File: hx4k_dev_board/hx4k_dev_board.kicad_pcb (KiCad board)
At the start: 4 copper layers, 85 x 54 mm, 111 parts, among them J1 USB_B, J2 RB1-125B8G1A, J3 Conn_01x08, J4 Conn_02x06_Odd_Even, J5 Conn_02x06_Odd_Even, SW1 SW_SPST, SW2 SW_SPST, SW3 SW_SPST, U1 W9812G6KH-6, U2 CH340E, U3 TPS7A7001DDA, U4 TPS7A7001DDA, U5 RTL8211EG-VB-CG, U6 ICE40HX4K-TQ144, U7 W25Q128JVS, X1 SG-7050CAN, X2 SG-7050CAN

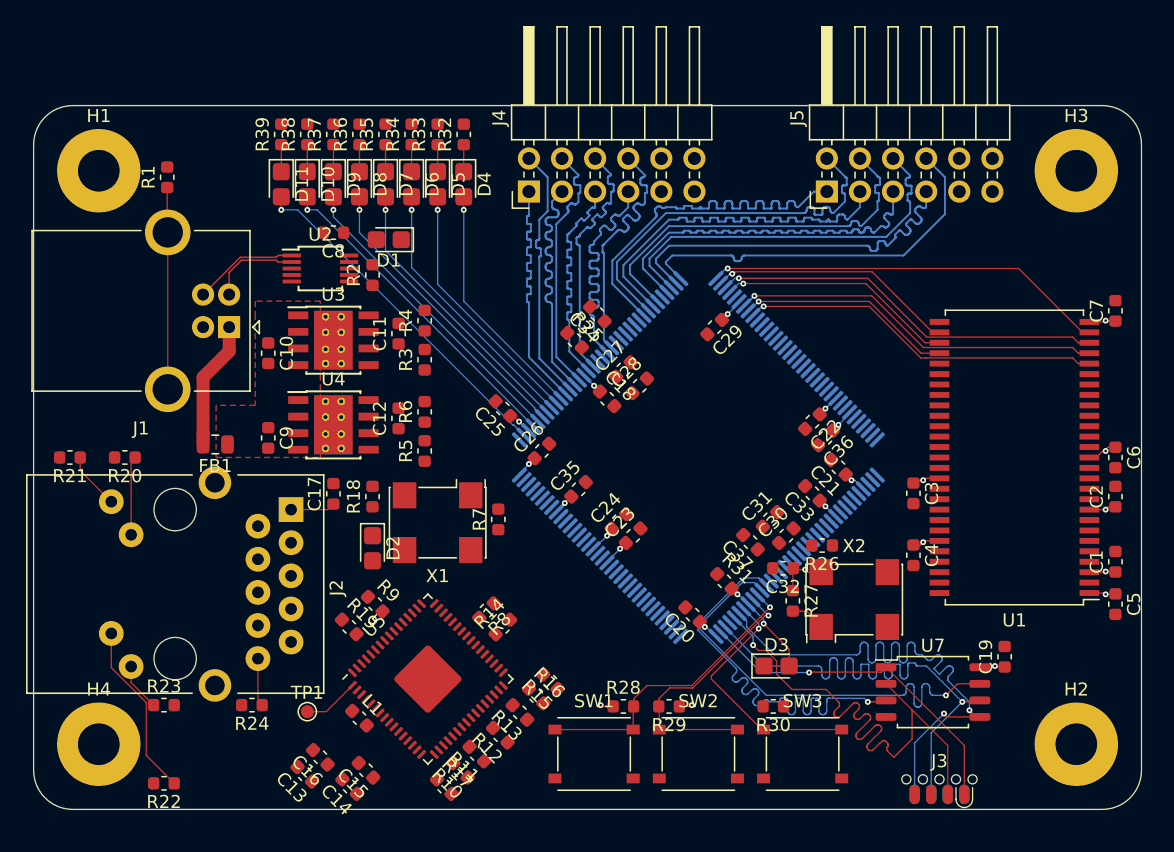
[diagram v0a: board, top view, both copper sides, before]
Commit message: Pre tuning of DDR length matching
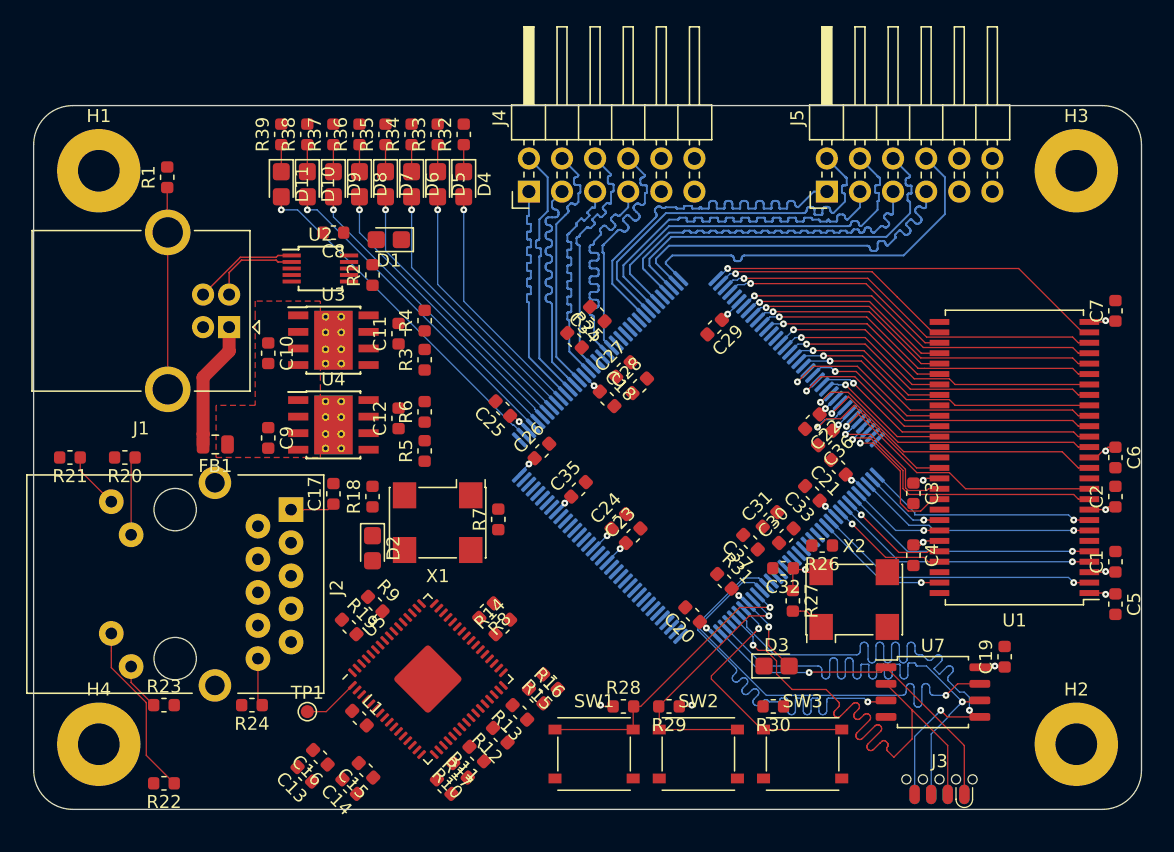
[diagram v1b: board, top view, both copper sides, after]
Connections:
- U6 pad 19: Net-(U6-Pad19) -> /SDRAM/~CS
- U6 pad 20: Net-(U6-Pad20) -> /FPGA/~RAM_RAS
- U6 pad 21: Net-(U6-Pad21) -> /SDRAM/CKE
- U6 pad 22: Net-(U6-Pad22) -> /SDRAM/~CAS
- U6 pad 23: Net-(U6-Pad23) -> /SDRAM/CLK
- U6 pad 24: Net-(U6-Pad24) -> /FPGA/~RAM_WE
- U6 pad 25: Net-(U6-Pad25) -> /FPGA/RAM_UDQM
- U6 pad 26: Net-(U6-Pad26) -> /SDRAM/LDQM
- U6 pad 28: Net-(U6-Pad28) -> /SDRAM/DATA7
- U6 pad 29: Net-(U6-Pad29) -> /SDRAM/DATA8
- U6 pad 31: Net-(U6-Pad31) -> /SDRAM/DATA6
- U6 pad 32: Net-(U6-Pad32) -> /SDRAM/DATA9
- U6 pad 33: Net-(U6-Pad33) -> /SDRAM/DATA5
- U6 pad 34: Net-(U6-Pad34) -> /SDRAM/DATA10
- U6 pad 37: Net-(U6-Pad37) -> /SDRAM/DATA4
- U6 pad 38: Net-(U6-Pad38) -> /SDRAM/DATA11
- U6 pad 39: /SDRAM/~CS -> /SDRAM/DATA3
- U6 pad 41: /SDRAM/CKE -> /SDRAM/DATA12
- U6 pad 42: /SDRAM/CLK -> /SDRAM/DATA2
- U6 pad 43: /SDRAM/LDQM -> /SDRAM/DATA13
- U6 pad 44: /FPGA/RAM_UDQM -> /SDRAM/DATA1
- U6 pad 45: /FPGA/~RAM_WE -> /SDRAM/DATA14
- U6 pad 47: /SDRAM/~CAS -> /SDRAM/DATA0
- U6 pad 48: /FPGA/~RAM_RAS -> /SDRAM/DATA15
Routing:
- net /SDRAM/ADDRESS10: track 0.00 -> 27.2 mm, vias 0 -> 1
- net /SDRAM/BS1: track 0.00 -> 25.9 mm, vias 0 -> 1
- net /SDRAM/BS0: track 0.00 -> 24.9 mm, vias 0 -> 1
- net /SDRAM/~CS: track 0.00 -> 24.0 mm, vias 0 -> 1
- net /FPGA/~RAM_RAS: track 0.00 -> 23.8 mm, vias 0 -> 1
- net /SDRAM/LDQM: track 0.00 -> 23.8 mm, vias 0 -> 1
- net /SDRAM/DATA7: track 0.00 -> 23.7 mm, vias 0 -> 1
- net /SDRAM/~CAS: track 0.00 -> 23.3 mm, vias 0 -> 1
- net /SDRAM/DATA6: track 0.00 -> 22.5 mm, vias 0 -> 1
- net /FPGA/~RAM_WE: track 0.00 -> 22.5 mm, vias 0 -> 1
- net /SDRAM/DATA5: track 0.00 -> 22.4 mm, vias 0 -> 1
- net /SDRAM/DATA0: track 0.00 -> 21.8 mm, vias 0 -> 1
- net /SDRAM/DATA1: track 0.00 -> 20.5 mm, vias 0 -> 1
- net /SDRAM/DATA2: track 0.00 -> 19.7 mm, vias 0 -> 1
- net /SDRAM/DATA3: track 0.00 -> 18.4 mm, vias 0 -> 1
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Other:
- net class 100R diff: via_dia 0.45 -> 0.53
- net class 50R: via_dia 0.45 -> 0.53
- net class 90R: via_dia 0.45 -> 0.53
- net class Default: via_dia 0.45 -> 0.53
- rule via_min_size: 0.45 -> 0.53

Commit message: Fully routed
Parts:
- removed R8: 10k, Resistor_SMD:R_0603_1608Metric
- U5: footprint Package_DFN_QFN:QFN-64-1EP_9x9mm_P0.5mm_EP3.8x3.8mm -> Package_DFN_QFN:QFN-64-1EP_9x9mm_P0.5mm_EP3.8x3.8mm_ThermalVias
- moved C14 12.7 mm to (316.9, 84.6), turned to 45 degrees
- moved R11 12.6 mm to (337.6, 88.0)
- moved R12 11.8 mm to (338.4, 86.5)
- moved R14 11.7 mm to (336.1, 75.7)
- moved R10 11.2 mm to (335.4, 90.3)
- moved C13 10.2 mm to (317.1, 86.7), turned to 45 degrees
- moved R25 8.28 mm to (340.6, 68.6), turned to 135 degrees
- moved R16 7.58 mm to (336.3, 84.4)
- moved R26 6.82 mm to (347.4, 75.7), turned to 315 degrees
- moved R13 6.16 mm to (334.9, 87.5)
- moved R15 4.36 mm to (335.5, 85.9)
- moved D1 4.22 mm to (323.1, 58.4)
- moved C15 3.34 mm to (316.9, 93.0)
- moved R9 2.61 mm to (321.6, 82.2), turned to 225 degrees
- moved R30 2.33 mm to (347.4, 91.3), turned to 0 degrees
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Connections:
- net /POWER/1V8FB renamed /POWER/1V2FB
- net Net-(C27-Pad1) renamed /FPGA/VCCPLL1
- net Net-(C27-Pad2) renamed /FPGA/GNDPLL1
- net Net-(C30-Pad1) renamed /FPGA/VCCPLL0
- net Net-(C30-Pad2) renamed /FPGA/GNDPLL0
- U6 pad 101: /ETHERNET/COL -> /FPGA/ETH_TXD6
- U6 pad 102: /ETHERNET/CS -> /FPGA/ETH_TXD7
- U6 pad 104: /FPGA/ETH_MDC -> /FPGA/ETH_TXER
- U6 pad 107: /FPGA/~ETH_PHYRST -> /FPGA/ETH_MDC
- U6 pad 73: /FPGA/ETH_GTXCLK -> /FPGA/ETH_RXDV
- U6 pad 74: /FPGA/ETH_TXCLK -> /FPGA/ETH_RXD0
- U6 pad 75: /FPGA/ETH_TXD0 -> /FPGA/ETH_RXD1
- U6 pad 76: /FPGA/ETH_TXD1 -> /FPGA/ETH_RXD2
- U6 pad 78: /FPGA/ETH_TXD2 -> /FPGA/ETH_RXD3
- U6 pad 79: /FPGA/ETH_TXD3 -> /ETHERNET/RXCLK
- U6 pad 80: /FPGA/ETH_TXD4 -> /FPGA/ETH_RXD4
- U6 pad 81: /FPGA/ETH_TXD5 -> /FPGA/ETH_RXD5
- U6 pad 82: /FPGA/ETH_TXD6 -> /FPGA/ETH_RXD6
- U6 pad 83: /FPGA/ETH_TXD7 -> /FPGA/ETH_RXD7
- U6 pad 84: /FPGA/ETH_TXEN -> /FPGA/ETH_RXER
- U6 pad 85: /FPGA/ETH_TXER -> /ETHERNET/COL
- U6 pad 87: /ETHERNET/RXCLK -> /ETHERNET/CS
- U6 pad 88: /FPGA/ETH_RXD0 -> /FPGA/ETH_GTXCLK
- U6 pad 90: /FPGA/ETH_RXD1 -> /FPGA/ETH_TXEN
- U6 pad 91: /FPGA/ETH_RXD2 -> /FPGA/ETH_TXD0
- U6 pad 93: /FPGA/ETH_RXD3 -> /FPGA/~ETH_PHYRST
- U6 pad 94: /FPGA/ETH_RXD4 -> /FPGA/ETH_TXD1
- U6 pad 95: /FPGA/ETH_RXD5 -> /FPGA/ETH_TXD2
- U6 pad 96: /FPGA/ETH_RXD6 -> /FPGA/ETH_TXD3
- U6 pad 97: /FPGA/ETH_RXD7 -> /FPGA/ETH_TXCLK
- U6 pad 98: /FPGA/ETH_RXDV -> /FPGA/ETH_TXD4
- U6 pad 99: /FPGA/ETH_RXER -> /FPGA/ETH_TXD5
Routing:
- net GND: track 0.00 -> 84.6 mm, vias 0 -> 74
- net /USB_UART/UART_RX: track 0.00 -> 48.1 mm, vias 0 -> 1
- net /FPGA/UART_CTS: track 0.00 -> 47.3 mm, vias 0 -> 1
- net /FPGA/~UART_RTS: track 0.00 -> 46.5 mm, vias 0 -> 1
- net /FPGA/UART_RX: track 0.00 -> 44.2 mm, vias 0 -> 1
- net +3V3: track 37.6 -> 68.7 mm, vias 19 -> 50
- net /ETHERNET/LED_G_HIGH: track 4.38 -> 34.0 mm
- net /ETHERNET/LED_Y_HIGH: track 13.5 -> 40.5 mm
- net /ETHERNET/MDI2_P: track 0.00 -> 25.7 mm, vias 0 -> 1
- net /FPGA/ETH_RXDV: track 0.00 -> 24.9 mm, vias 0 -> 1
- net /SDRAM/DATA11: track 6.41 -> 31.2 mm
- net /FPGA/ETH_MDC: track 0.00 -> 24.2 mm, vias 0 -> 1
- net /SDRAM/DATA12: track 7.36 -> 31.0 mm
- net /FPGA/~ETH_PME_INT: track 0.00 -> 23.6 mm, vias 0 -> 1
- net /ETHERNET/MDI2_N: track 0.00 -> 23.3 mm, vias 0 -> 1
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- added copper zone on B.Cu, net +1V2
- added copper zone on F.Cu, net +1V2
- added copper zone on F.Cu, net +3V3
- added copper zone on In2.Cu, net +3V3
- added copper zone on F.Cu, net /ETHERNET/VDD
- added copper zone on F.Cu, net GND
- added copper zone on In1.Cu, net GND
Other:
- net class Power added: clearance 0.0889, trace_width 0.3, via_dia 0.53, via_drill 0.2

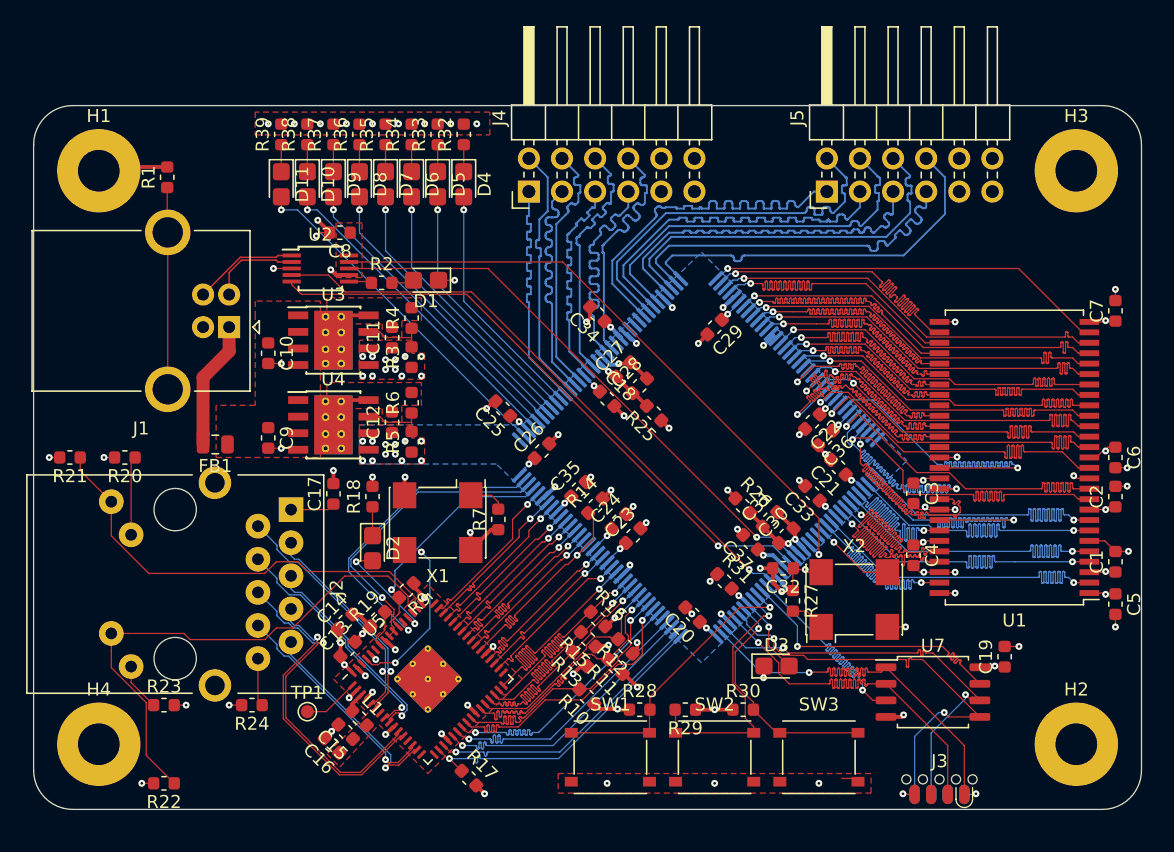
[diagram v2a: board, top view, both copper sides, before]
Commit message: PMODs corrected
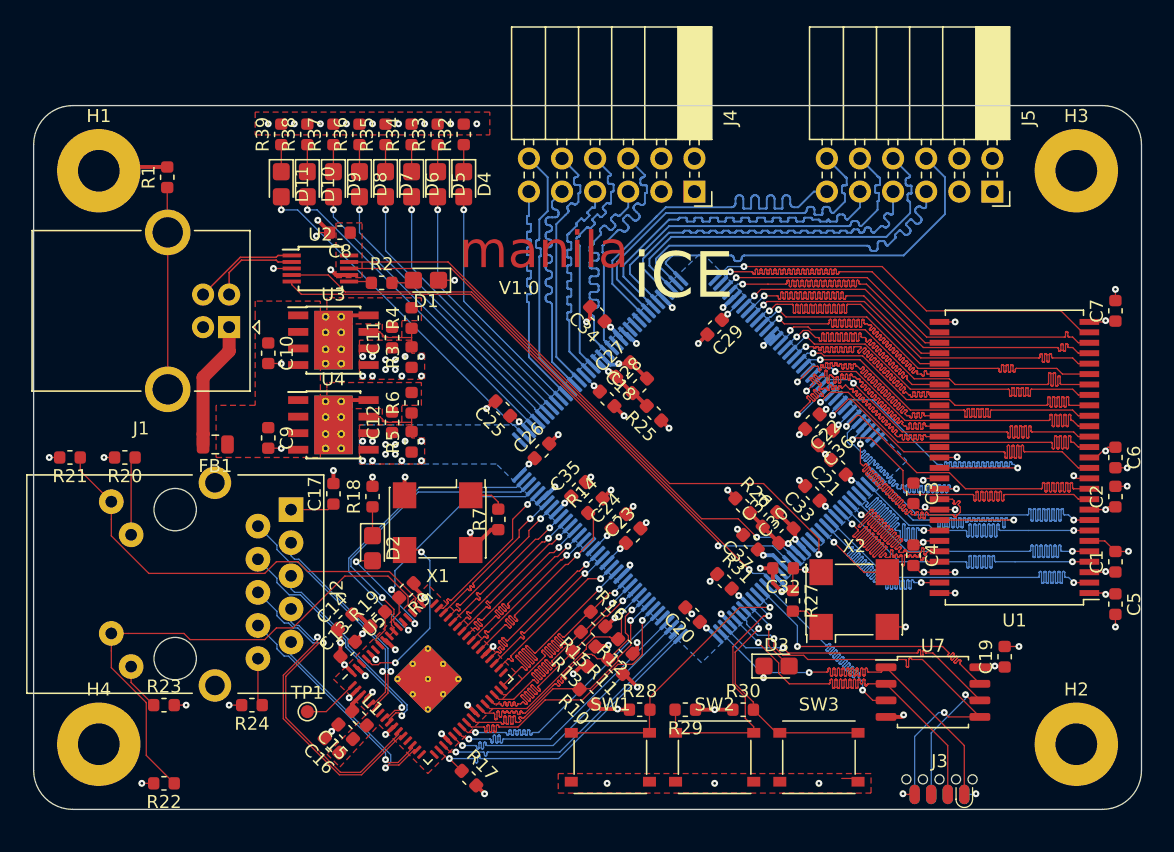
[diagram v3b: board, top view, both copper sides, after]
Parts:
- J4, J5: footprint Connector_PinHeader_2.54mm:PinHeader_2x06_P2.54mm_Horizontal -> Connector_PinSocket_2.54mm:PinSocket_2x06_P2.54mm_Horizontal
- moved J4 12.7 mm to (343.7, 51.6), turned to 270 degrees
- moved J5 12.7 mm to (366.6, 51.6), turned to 270 degrees
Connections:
- J4 pad 1: /PMODA/DATA0 -> +3V3
- J4 pad 10: GND -> /PMODA/DATA3
- J4 pad 11: +3V3 -> /PMODA/DATA0
- J4 pad 12: +3V3 -> /PMODA/DATA1
- J4 pad 2: /PMODA/DATA1 -> +3V3
- J4 pad 3: /PMODA/DATA2 -> GND
- J4 pad 4: /PMODA/DATA3 -> GND
- J4 pad 5: /PMODA/DATA4 -> /PMODA/DATA6
- J4 pad 6: /PMODA/DATA5 -> /PMODA/DATA7
- J4 pad 7: /PMODA/DATA6 -> /PMODA/DATA4
- J4 pad 8: /PMODA/DATA7 -> /PMODA/DATA5
- J4 pad 9: GND -> /PMODA/DATA2
- J5 pad 1: /PMODB/DATA0 -> +3V3
- J5 pad 10: GND -> /PMODB/DATA3
- J5 pad 11: +3V3 -> /PMODB/DATA0
- J5 pad 12: +3V3 -> /PMODB/DATA1
- J5 pad 2: /PMODB/DATA1 -> +3V3
- J5 pad 3: /PMODB/DATA2 -> GND
- J5 pad 4: /PMODB/DATA3 -> GND
- J5 pad 5: /PMODB/DATA4 -> /PMODB/DATA6
- J5 pad 6: /PMODB/DATA5 -> /PMODB/DATA7
- J5 pad 7: /PMODB/DATA6 -> /PMODB/DATA4
- J5 pad 8: /PMODB/DATA7 -> /PMODB/DATA5
- J5 pad 9: GND -> /PMODB/DATA2
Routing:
- net /SDRAM/ADDRESS11: track 28.0 -> 31.2 mm
- net /SDRAM/CKE: track 28.6 -> 31.1 mm
- net /SDRAM/ADDRESS4: track 32.6 -> 31.0 mm
- net /USB_UART/UART_RX: track 48.1 -> 47.2 mm
- net /SDRAM/ADDRESS8: track 31.0 -> 32.0 mm
- net /SDRAM/~CS: track 31.1 -> 31.7 mm
- net /FPGA/~RAM_RAS: track 31.1 -> 31.6 mm
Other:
- board text added: "V1.0"
- board text added: "iCE"
- board text added: "manila"

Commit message: Basically done.
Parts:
- added G***: LOGO, Art:Shetland_combined, B.Cu at (370.0, 66.5)
- added REF**: KiCad-Logo2_5mm_SilkScreen, Symbol:KiCad-Logo2_5mm_SilkScreen, B.Cu at (309.0, 94.5)
- added REF**: OSHW-Logo_5.7x6mm_SilkScreen, Symbol:OSHW-Logo_5.7x6mm_SilkScreen, F.Cu at (368.2, 57.0)
- added TP2: TestPoint, TestPoint:TestPoint_Pad_D1.0mm, F.Cu at (326.5, 65.2)
- added TP3: TestPoint, TestPoint:TestPoint_Pad_D1.0mm, F.Cu at (326.8, 71.5)
- added TP4: TestPoint, TestPoint:TestPoint_Pad_D1.0mm, F.Cu at (294.0, 69.2)
- moved H2 44.0 mm to (373.0, 50.0)
- moved H3 44.0 mm to (373.0, 94.0)
- moved R1 4.69 mm to (306.6, 53.8), turned to 0 degrees
- moved R22 4.50 mm to (303.0, 92.5), turned to 0 degrees
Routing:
- net /VBUS: track 9.83 -> 21.8 mm
- net /ETHERNET/LED_Y_HIGH: track 40.5 -> 35.4 mm
- net GND: track 84.6 -> 80.5 mm, vias 74 -> 75
- net +1V2: track 8.97 -> 13.0 mm
- net +3V3: track 68.7 -> 72.4 mm
- net Net-(J1-Pad5): track 15.5 -> 15.0 mm
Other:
- board text added: "0"
- board text added: "1"
- board text added: "1V2"
- board text added: "2"
- board text added: "3"
- board text added: "3V3"
- board text added: "4"
- board text added: "5"
- board text added: "6"
- board text added: "7"
- board text added: "< PMOD0"
- board text added: "CRESET"
- board text added: "JLCJLCJLCJLC"
- board text added: "LEDs"
- board text added: "PMOD1 >"
- board text added: "SW0"
- board text added: "SW1"
- board text added: "Shetland"
- board text added: "VIN"

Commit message: Update
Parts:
- added R8: 91, Resistor_SMD:R_0603_1608Metric, F.Cu at (318.0, 82.5)
- C1, C2, C3, C4, C5, C6, C7: value 100nF -> 100n
- R19: value 2k49 -> 2k4
- moved C14 0.10 mm to (316.9, 84.7)
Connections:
- R19 pad 1: GND -> Net-(R19-Pad1)
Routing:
- net Net-(R19-Pad1): track 0.00 -> 2.07 mm
- net GND: track 80.5 -> 82.1 mm, vias 75 -> 76
